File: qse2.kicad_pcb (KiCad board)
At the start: 2 copper layers, 100 x 75 mm, 71 parts, among them J1 5-1814832-1, J2 5-1814832-1, J3 Conn_02x08_Odd_Even, J4 SJ-3524-SMT, J6 Conn_01x02, U1 SN74LVC1G14DBV, U2 SN74LVC1G14DBV, U3 SN74CBT3253, U4 SN74AC74PW, U5 AD8137ARZ-R7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

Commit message: Final gerbers before June release to PCB.
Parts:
- added C11: 1uF, Capacitor_SMD:C_1206_3216Metric, F.Cu at (127.5, 68.8)
- added C12: 0.1uF, Capacitor_SMD:C_1206_3216Metric, F.Cu at (195.0, 81.1)
- added C13: 1uF, Capacitor_SMD:C_1206_3216Metric, F.Cu at (126.3, 78.5)
- added C7: 0.1uF, Capacitor_SMD:C_1206_3216Metric, F.Cu at (154.1, 52.2)
- added C9: 0.1uF, Capacitor_SMD:C_1206_3216Metric, B.Cu at (139.2, 66.2)
- added J7: B4B-XH-A_LF__SN_, digikey-footprints:PinHeader_1x4_P2.5mm_Drill1.1mm, F.Cu at (195.0, 86.6)
- added U10: SN74LVC1G14DBV, Package_TO_SOT_SMD:SOT-23-5, F.Cu at (151.2, 51.4)
- added U11: NCP508SQ33T1G, 16TSOP:TSOP-5-483-N_ONS, F.Cu at (127.7, 73.0)
- R5, R7: value 1000 -> 4.7k
- moved R5 40.0 mm to (120.2, 61.8), turned to 180 degrees
- moved R7 33.8 mm to (120.2, 64.7), turned to 180 degrees
- moved C6 2.99 mm to (154.1, 58.1), turned to 90 degrees
- moved C4 1.80 mm to (120.3, 67.6), turned to 0 degrees
- moved TP2 0.19 mm to (149.7, 58.7)
- moved U2 0.10 mm to (151.2, 55.6)
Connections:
- C1 pad 2: /5V_FILT -> /3_3V
- C10 pad 2: /5V_FILT -> /3_3V
- C22 pad 2: /5V_FILT -> /3_3V
- C6 pad 2: /5V_FILT -> /3_3V
- J1 pad 2: /CLK1 -> Net-(J1-Pad2)
- J3 pad 3: unconnected-(J3-Pin_3-Pad3) -> /SDA
- J3 pad 4: unconnected-(J3-Pin_4-Pad4) -> /SCL
- R5 pad 1: GND -> /3_3V
- R5 pad 2: Net-(U6-EN) -> /SDA
- R7 pad 1: Net-(U6-EN) -> /3_3V
- R7 pad 2: /5V_FILT -> /SCL
- U1 pad 5: /5V_FILT -> /3_3V
- U2 pad 5: /5V_FILT -> /3_3V
- U4 pad 1: /5V_FILT -> /3_3V
- U4 pad 13: /5V_FILT -> /3_3V
- U4 pad 14: /5V_FILT -> /3_3V
- U6 pad 3: Net-(U6-EN) -> /5V_FILT
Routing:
- net /SDA: track 0.00 -> 143.1 mm
- net /SCL: track 0.00 -> 140.8 mm
- net /3_3V: track 0.00 -> 81.6 mm, vias 0 -> 5
- net /5V_FILT: track 160.8 -> 208.3 mm, vias 9 -> 7
- net GND: track 22.0 -> 33.3 mm, vias 135 -> 147
- net Net-(U6-EN): track 7.68 -> 0.00 mm
- net /CLK1: track 24.1 -> 17.5 mm
- net Net-(J1-Pad2): track 0.00 -> 5.15 mm
- net /FB1: track 13.9 -> 13.4 mm
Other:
- board text added: "V1.1"
- board text removed: "V1.0"

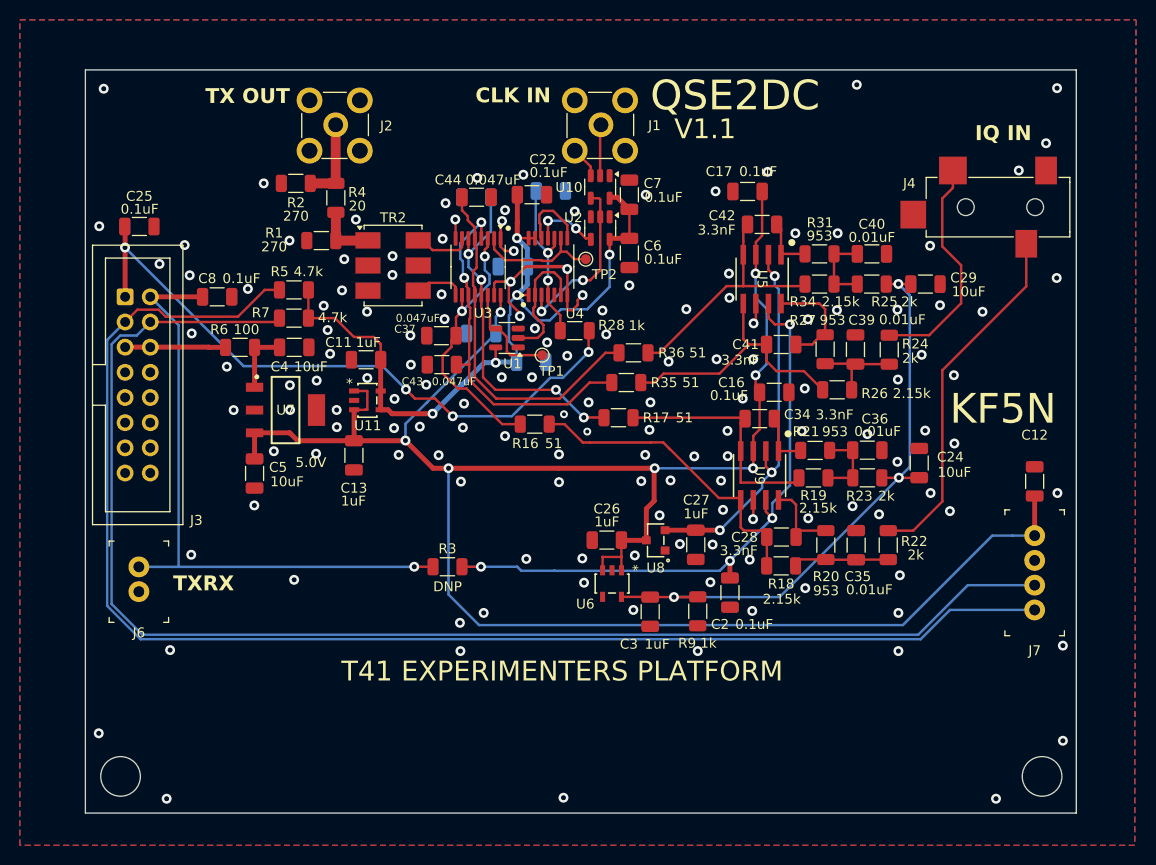
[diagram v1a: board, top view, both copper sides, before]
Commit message: Mostly cleaned up version with SOICs replacing TSOPs.
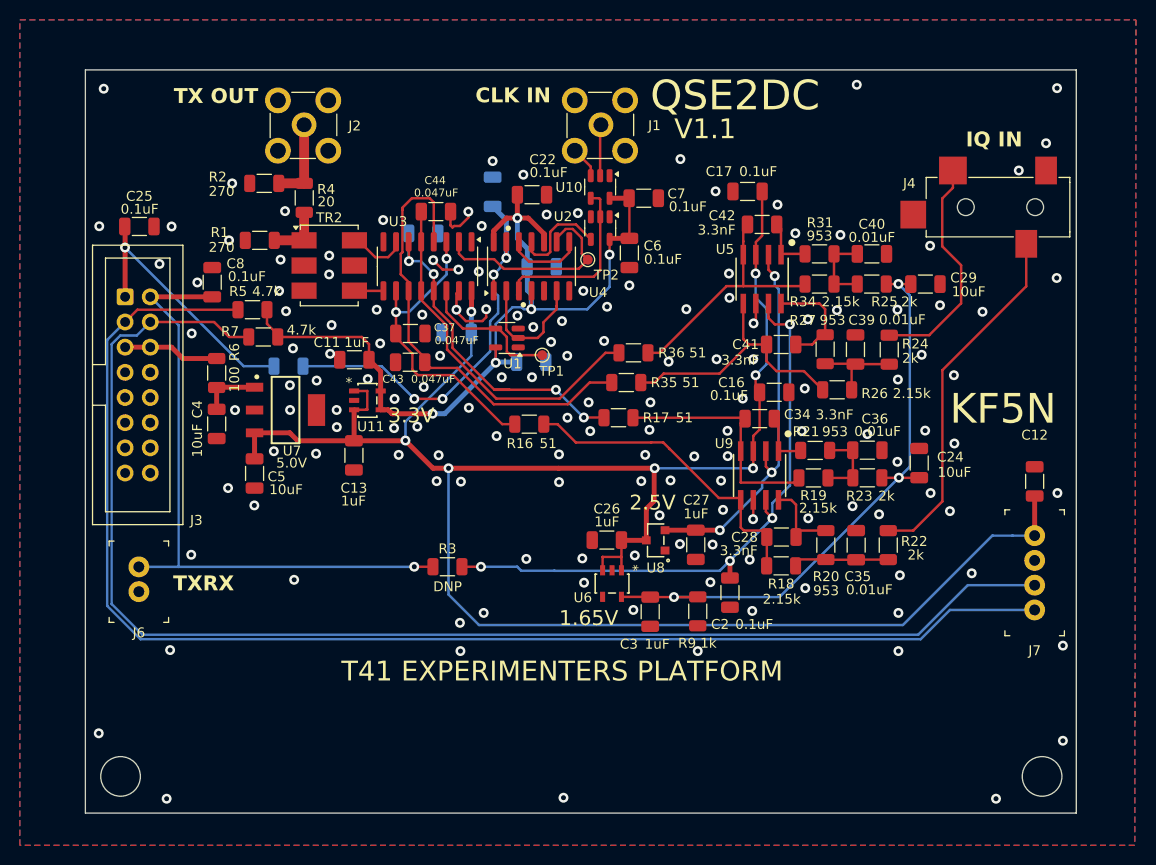
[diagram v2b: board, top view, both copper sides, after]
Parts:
- R28: moved to B.Cu
- U3: footprint Package_SO:TSSOP-16_4.4x5mm_P0.65mm -> Package_SO:SOIC-16_3.9x9.9mm_P1.27mm
- U4: footprint Package_SO:TSSOP-14_4.4x5mm_P0.65mm -> Package_SO:SOIC-14_3.9x8.7mm_P1.27mm
- moved R28 29.1 mm to (119.7, 69.5), turned to 0 degrees
- moved C4 11.0 mm to (112.5, 75.3), turned to -90 degrees
- moved C38 6.48 mm to (133.3, 56.1), turned to 0 degrees
- moved TR2 6.44 mm to (123.8, 59.3)
- moved R1 6.21 mm to (116.8, 56.8)
- moved C31 5.88 mm to (140.3, 51.9), turned to -90 degrees
- moved U3 5.11 mm to (133.7, 59.4)
- moved R5 4.64 mm to (116.1, 63.8)
- moved C44 4.36 mm to (134.6, 53.9)
- moved R7 3.64 mm to (117.2, 66.5)
- moved R6 3.50 mm to (112.5, 70.2), turned to -90 degrees
- moved C43 3.21 mm to (132.0, 69.1)
- moved J2 3.19 mm to (121.2, 45.2)
- moved R2 3.19 mm to (117.2, 51.0)
- moved R4 3.19 mm to (121.3, 52.5)
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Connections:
- net /SET renamed /CLEAR
- C31 pad 2: /PREN -> /CLRN
- R28 pad 2: /PREN -> /CLRN
- U4 pad 1: /3_3V -> /CLRN
- U4 pad 10: /PREN -> /3_3V
- U4 pad 13: /3_3V -> /CLRN
- U4 pad 4: /PREN -> /3_3V
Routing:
- net /CLRN: track 0.00 -> 41.8 mm, vias 0 -> 4
- net /CLEAR: track 65.9 -> 27.1 mm, vias 4 -> 1
- net /PREN: track 16.8 -> 0.00 mm, vias 2 -> 0
- net GND: track 33.3 -> 21.0 mm, vias 147 -> 149
- net Net-(U3-1B3): track 36.4 -> 45.9 mm, vias 2 -> 0
- net /LO_Q: track 12.9 -> 21.3 mm
- net /3_3V: track 81.6 -> 89.7 mm
- net /SDA: track 143.1 -> 137.5 mm
- net /LO_I: track 10.6 -> 14.5 mm
- net Net-(U3-1B4): track 27.4 -> 31.3 mm
- net /CLK2: track 6.81 -> 10.2 mm, vias 2 -> 0
- net /SCL: track 140.8 -> 138.1 mm
- net Net-(U3-2A): track 5.17 -> 2.94 mm
- net /5V_FILT: track 208.3 -> 206.9 mm
- net /TXRX: track 63.4 -> 64.1 mm
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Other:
- board text added: "1.65V"
- board text added: "2.5V"
- board text added: "3.3V"

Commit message: Ready to release V1.1 June 30.
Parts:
- added C14: 10uF, Capacitor_SMD:C_1206_3216Metric, F.Cu at (186.5, 79.3)
- added C15: 10uF, Capacitor_SMD:C_1206_3216Metric, F.Cu at (183.9, 64.2)
- moved C29 0.21 mm to (184.0, 61.0)
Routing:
- net /REF1.6: track 62.6 -> 68.9 mm
- net Net-(J4-Pad2): track 23.2 -> 24.6 mm
- net Net-(J4-Pad3): track 36.2 -> 37.1 mm
- net GND: vias 149 -> 150

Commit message: Updated README and very minor update to Gerbers.
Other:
- board text added: "QSE2DCEZ"
- board text removed: "QSE2DC"
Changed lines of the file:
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@@
 	(paper "A4")
 	(title_block
-		(title "QSD Divide by Two")
-		(date "2023-07-26")
+		(title "QSE2DCEZ Divide by Two")
+		(date "2024-07-26")
 	)
 	(layers
@@
 		(tags "capacitor")
 		(property "Reference" "C15"
-			(at -3.9 0.75 360)
+			(at -3.9 0.75 0)
 			(layer "F.SilkS")
 			(effects
@@
 		)
 		(fp_text user "${REFERENCE}"
-			(at 0 0 360)
+			(at 0 0 0)
 			(layer "F.Fab")
 			(effects
@@
 		)
 		(property "Value" "NCP115ASN330T2G"
-			(at 0 0 270)
+			(at 0 0 -90)
 			(unlocked yes)
 			(layer "F.Fab")
@@
 		)
 		(fp_text user "*"
-			(at -1.59385 -2.601 270)
+			(at -1.59385 -2.601 -90)
 			(layer "F.SilkS")
 			(effects
@@
 		)
 		(fp_text user "*"
-			(at -0.5715 -1.5088 270)
+			(at -0.5715 -1.5088 -90)
 			(layer "F.Fab")
 			(hide yes)
@@
 		)
 	)
-	(gr_text "QSE2DC"
+	(gr_text "QSE2DCEZ"
 		(at 156.21 43.942 0)
 		(layer "F.SilkS")
